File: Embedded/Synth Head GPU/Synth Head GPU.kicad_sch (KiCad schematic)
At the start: 0 parts

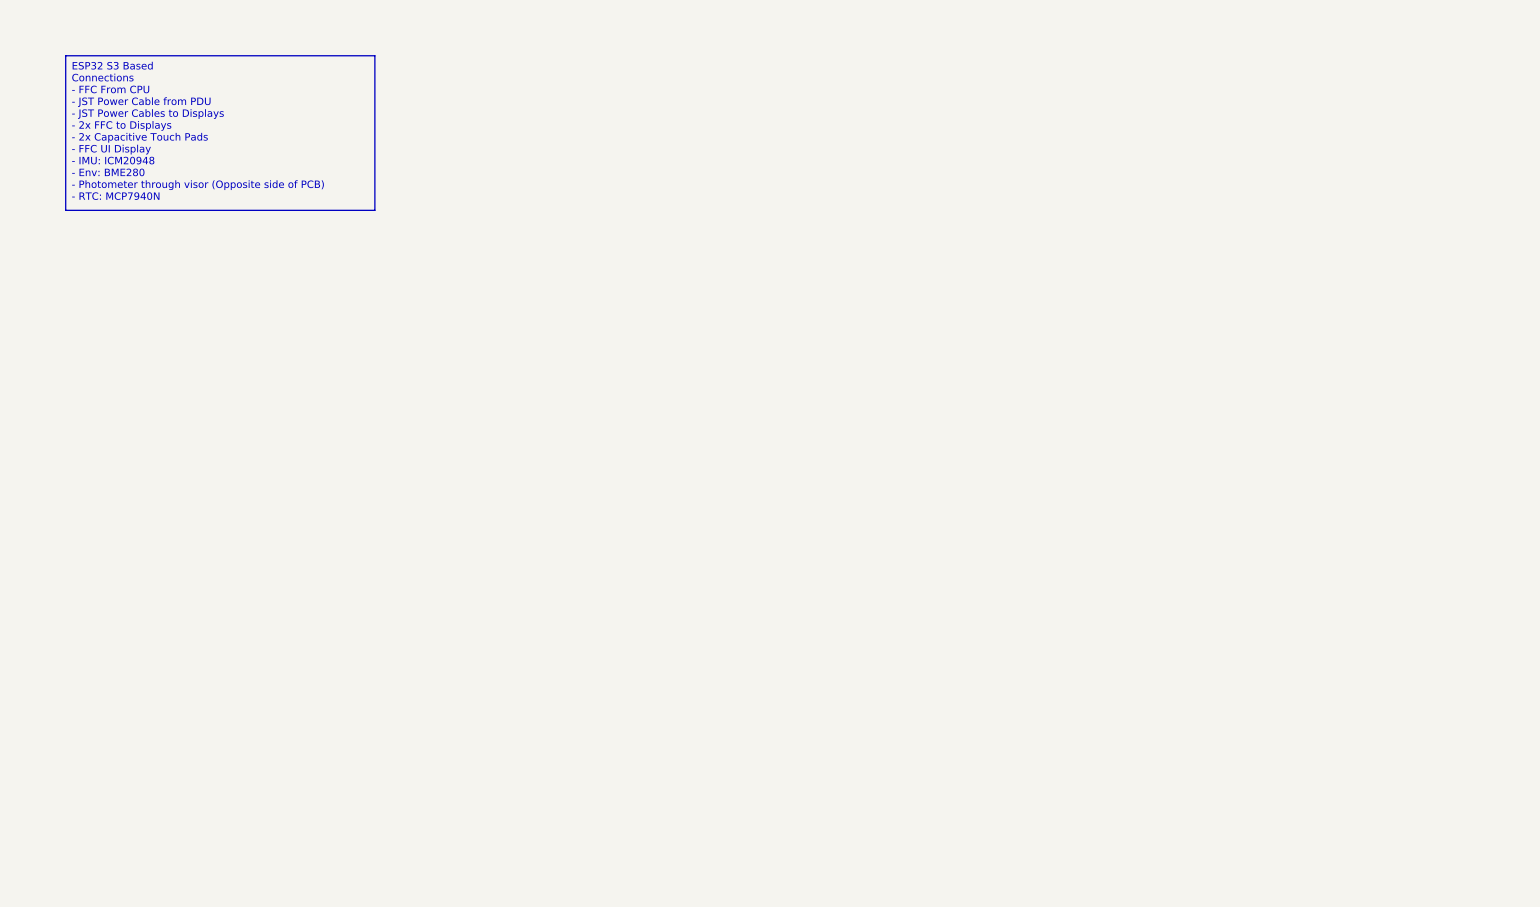
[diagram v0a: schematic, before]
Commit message: KiCAD Added the schematics to drive some sensors
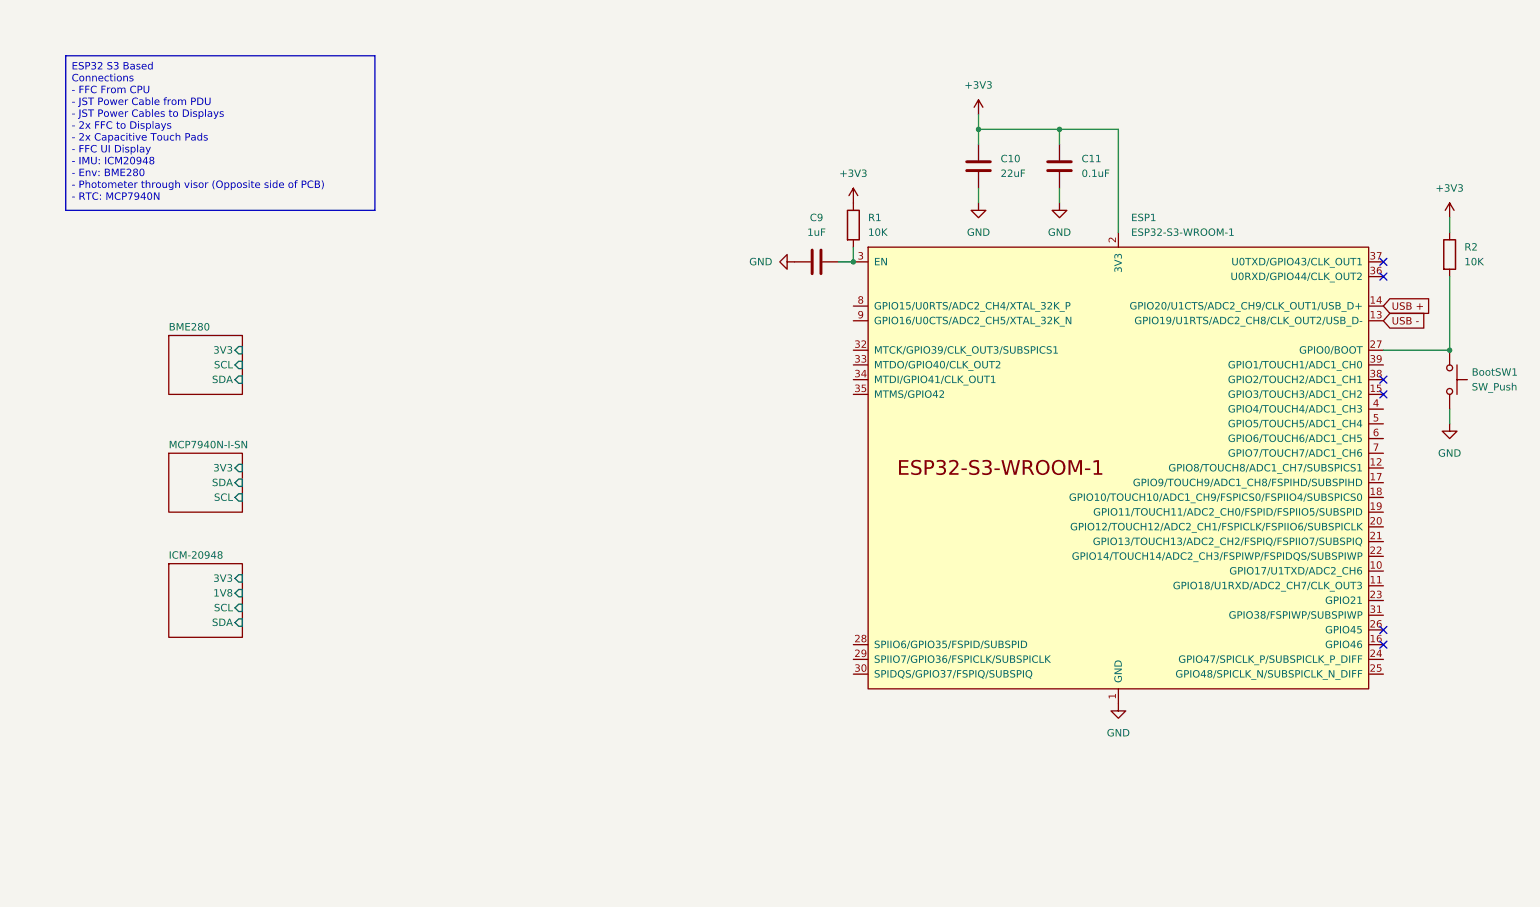
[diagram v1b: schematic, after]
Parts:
- added BootSW1: SW_Push, Button-R-667843:Button-R-667843, symbol Switch:SW_Push
- added C10: 22uF, Capacitor_SMD:C_0603_1608Metric_Pad1.08x0.95mm_HandSolder, symbol Device:C
- added C11: 0.1uF, Capacitor_SMD:C_0603_1608Metric, symbol Device:C
- added C9: 1uF, Capacitor_SMD:C_0603_1608Metric, symbol Device:C
- added ESP1: ESP32-S3-WROOM-1, PCM_Espressif:ESP32-S3-WROOM-1U, symbol PCM_Espressif:ESP32-S3-WROOM-1
- added R1, R2: 10K, Resistor_SMD:R_0603_1608Metric, symbol Device:R
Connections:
- new net: C9.2, ESP1.3 (EN), R1.2
- new net: BootSW1.1, ESP1.27 (GPIO0/BOOT), R2.2
- new net +3V3: C10.1, C11.1, ESP1.2 (3V3), R1.1, R2.1
- new net GND: BootSW1.2, C10.2, C11.2, C9.1, ESP1.1 (GND), ESP1.40 (GND), ESP1.41 (GND)
- new net USB +: ESP1.14 (GPIO20/U1CTS/ADC2_CH9/CLK_OUT1/USB_D+)
- new net USB -: ESP1.13 (GPIO19/U1RTS/ADC2_CH8/CLK_OUT2/USB_D-)
- no-connect marks 0 -> 6
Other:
- added sheet BME280 (BME280.kicad_sch)
- added sheet ICM-20948 (ICM20948.kicad_sch)
- added sheet MCP7940N-I-SN (MCP7940N-SN.kicad_sch)

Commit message: Some Sensors Added to the GPU and CPU
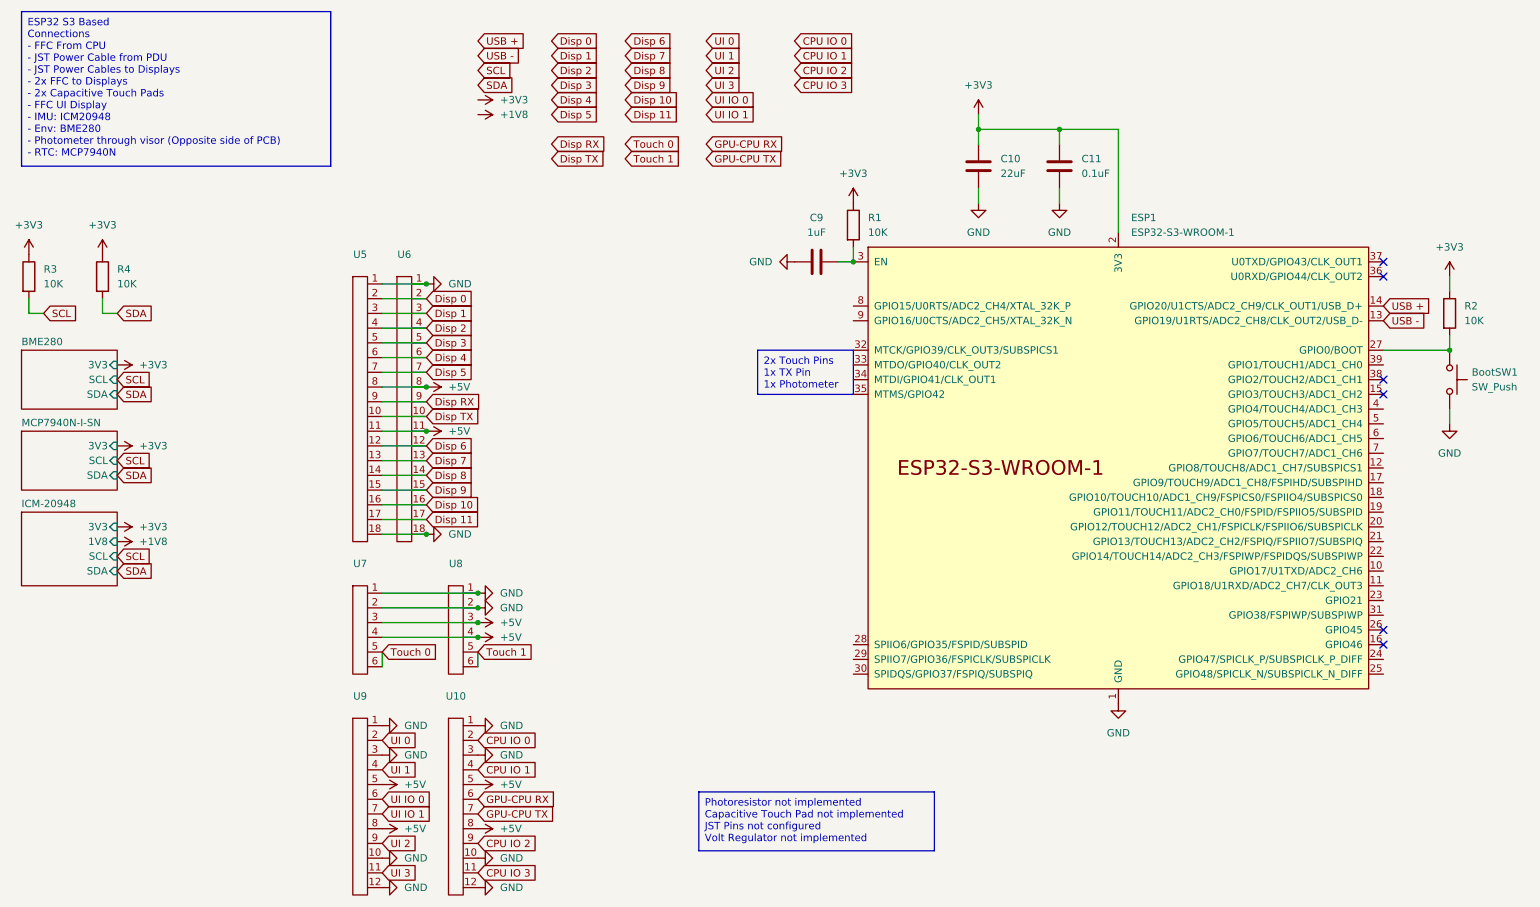
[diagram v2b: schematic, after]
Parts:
- added R3, R4: 10K, symbol Device:R
- added U10, U9: ~, symbol FCC_Connector:FFC_12P
- added U5, U6: ~, FFC_Connector:FFC Aliexpress 0.5mm 18P, symbol FCC_Connector:FFC_18P
- added U7, U8: ~, symbol FCC_Connector:FFC_6P
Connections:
- net +3V3: now also R3.1, R4.1
- net GND: now also U10.1, U10.10, U10.12, U10.3, U5.1, U5.18, U6.1, U6.18, U7.1, U7.2, U8.1, U8.2, U9.1, U9.10, U9.12, U9.3
- new net +5V: U10.5, U10.8, U5.11, U5.8, U6.11, U6.8, U7.3, U7.4, U8.3, U8.4, U9.5, U9.8
- new net CPU IO 0: U10.2
- new net CPU IO 1: U10.4
- new net CPU IO 2: U10.9
- new net CPU IO 3: U10.11
- new net Disp 0: U5.2, U6.2
- new net Disp 1: U5.3, U6.3
- new net Disp 10: U5.16, U6.16
- new net Disp 11: U5.17, U6.17
- new net Disp 2: U5.4, U6.4
- new net Disp 3: U5.5, U6.5
- new net Disp 4: U5.6, U6.6
- new net Disp 5: U5.7, U6.7
- new net Disp 6: U5.12, U6.12
- new net Disp 7: U5.13, U6.13
- new net Disp 8: U5.14, U6.14
- new net Disp 9: U5.15, U6.15
- new net Disp RX: U5.9, U6.9
- new net Disp TX: U5.10, U6.10
- new net GPU-CPU RX: U10.6
- new net GPU-CPU TX: U10.7
- new net SCL: R3.2
- new net SDA: R4.2
- new net Touch 0: U7.5, U7.6
- new net Touch 1: U8.5, U8.6
- new net UI 0: U9.2
- new net UI 1: U9.4
- new net UI 2: U9.9
- new net UI 3: U9.11
- new net UI IO 0: U9.6
- new net UI IO 1: U9.7
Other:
- moved on the sheet: R2

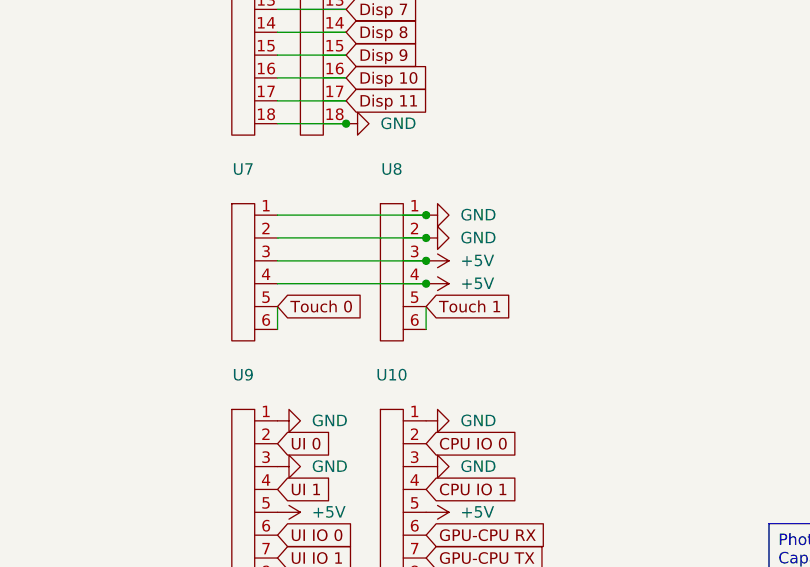
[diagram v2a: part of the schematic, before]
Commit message: Majority of the pins for the Mask Board & Snoot Added
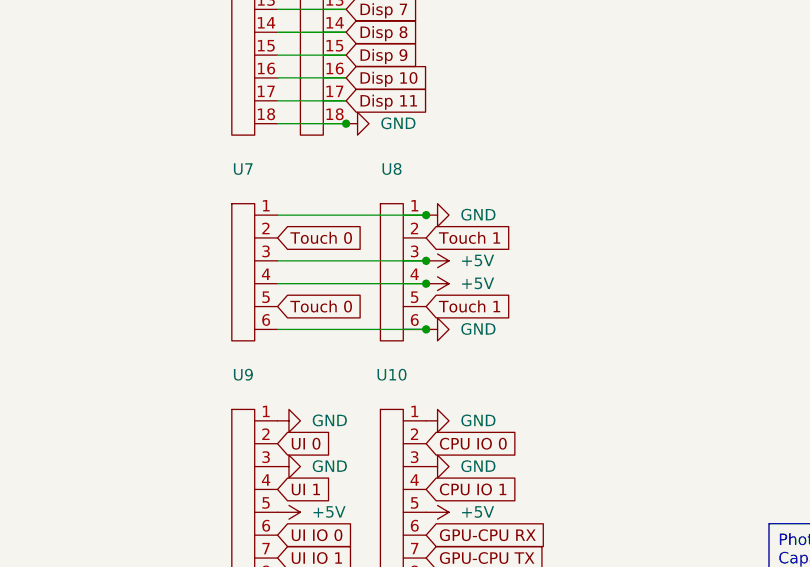
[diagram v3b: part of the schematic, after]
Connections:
- net GND: now also U7.6, U8.6; no longer U7.2, U8.2
- net Touch 0: now also U7.2; no longer U7.6
- net Touch 1: now also U8.2; no longer U8.6
